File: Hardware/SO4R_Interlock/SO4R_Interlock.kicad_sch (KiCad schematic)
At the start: 143 parts, among them J1 USB-C 2.0 16P, J2 USB-C 2.0 16P, J3 USB-C 2.0 16P, J4 USB-C 2.0 16P, J5 Header 1x3, J6 RJ45_LED_Shielded, J7 8P8C_LED_Shielded_x4, Q1 2N7002, Q2 2N7002, Q3 2N7002, Q4 2N7002, Q5 2N7002, Q6 2N7002, Q7 2N7002, Q8 2N7002, U1 FT230XS, U10 TPD4E02B04DQA, U11 TPD4E02B04DQA, U12 TPD4E02B04DQA, U2 FT230XS, U3 FT230XS, U4 FT230XS, U5 74LVC1G07, U6 74LVC1G07, U7 74LVC1G07, U8 AVR32DB48x-xPT, U9 TPD4E02B04DQA

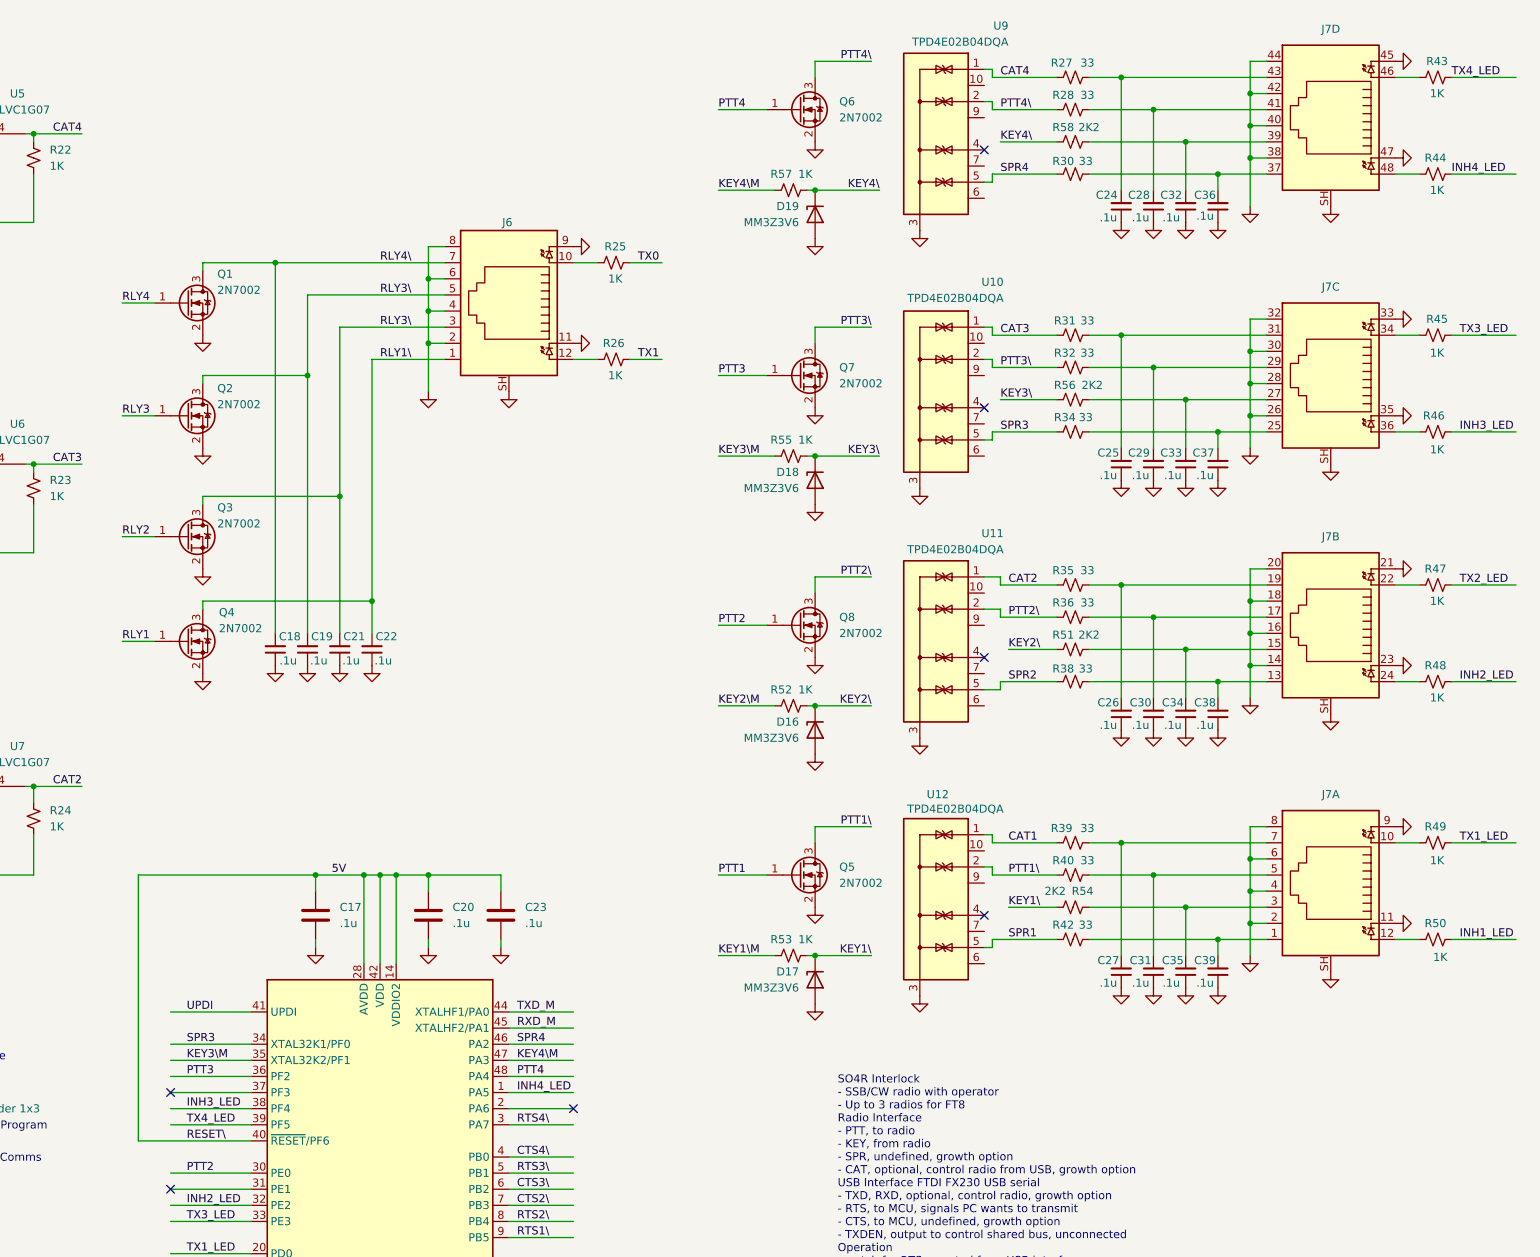
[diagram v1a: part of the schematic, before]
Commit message: reversed the RJ45 connectors
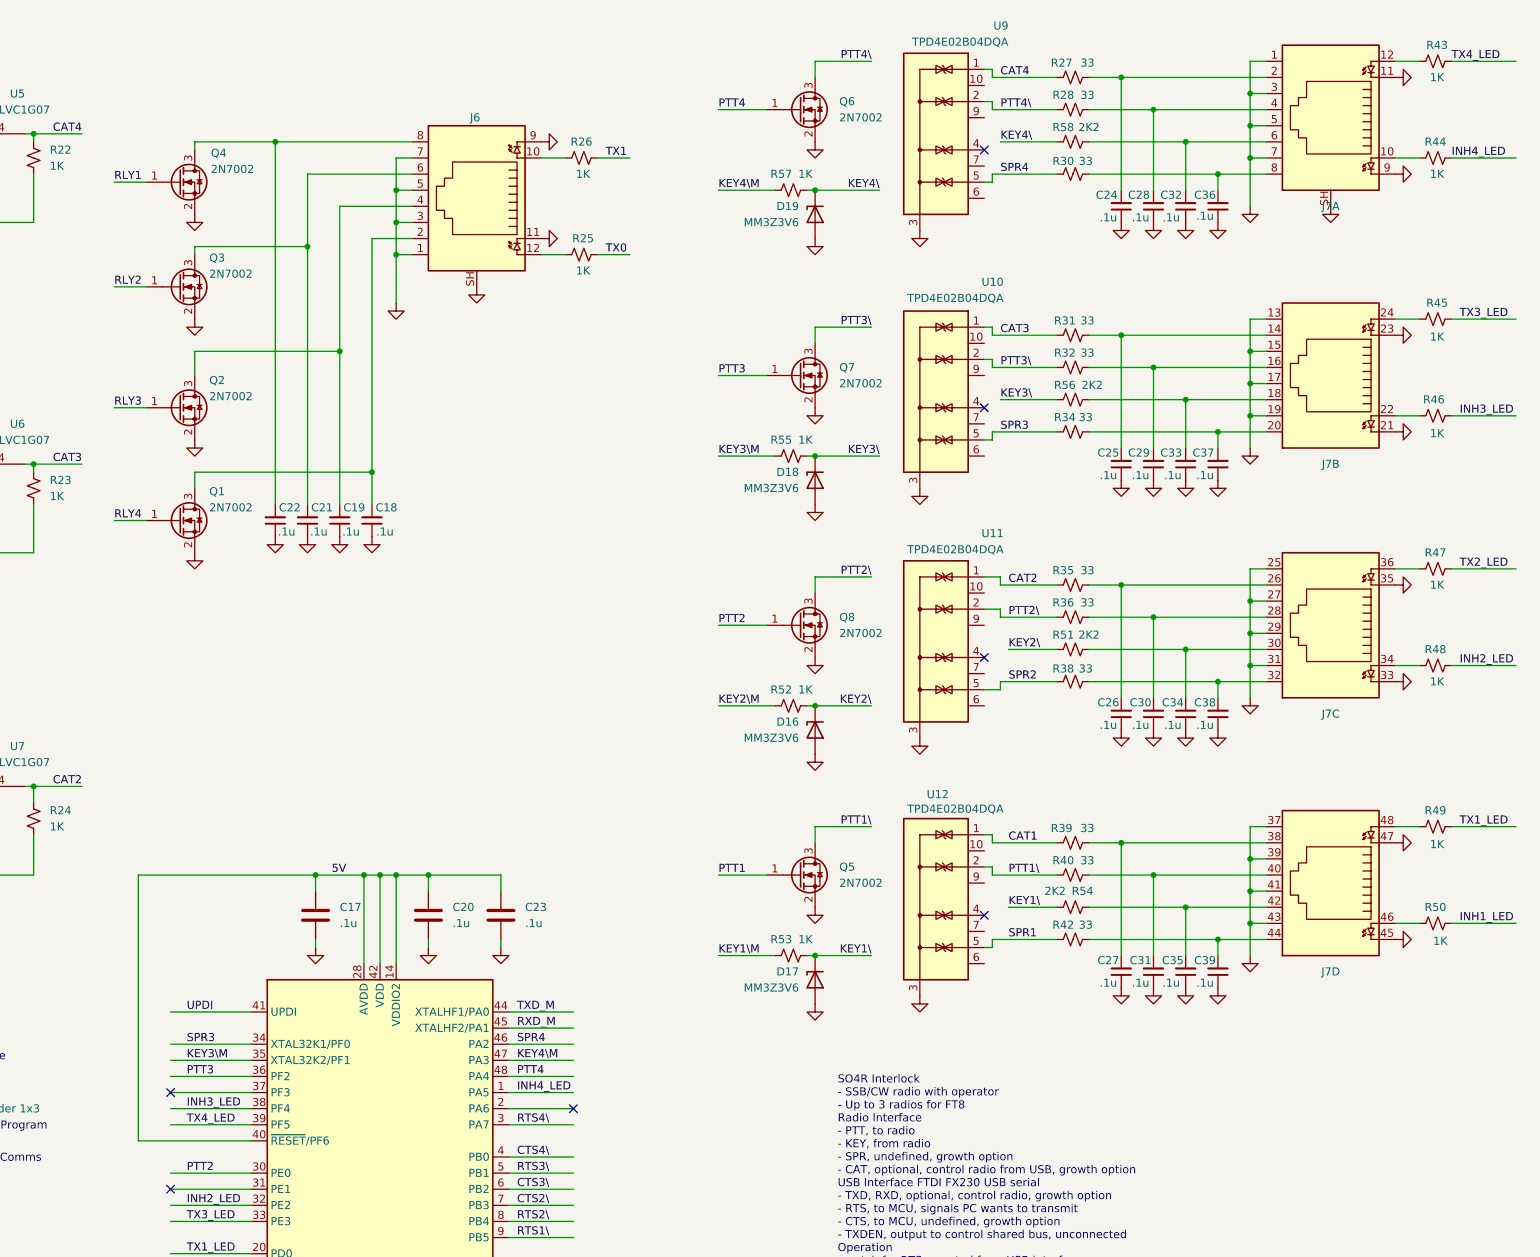
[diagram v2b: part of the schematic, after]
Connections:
- net GND: now also J6.1, J6.3, J6.5, J6.7, J7.1, J7.13, J7.15, J7.17, J7.19, J7.25, J7.27, J7.29, J7.3, J7.31, J7.37, J7.39, J7.41, J7.43, J7.5, J7.7; no longer J6.2, J6.4, J6.6, J6.8, J7.14, J7.16, J7.18, J7.2, J7.20, J7.26, J7.28, J7.30, J7.32, J7.38, J7.4, J7.40, J7.42, J7.44, J7.6, J7.8, J7.SH, J7.SH, J7.SH
- net at C25.2, R31.2: now also J7.14; no longer J7.31
- net at C38.2, R38.2: now also J7.32; no longer J7.13
- net at C34.2, R51.1: now also J7.30; no longer J7.15
- net at C30.2, R36.2: now also J7.28; no longer J7.17
- net at C26.2, R35.2: now also J7.26; no longer J7.19
- net at J7.22: now also R46.1; no longer R47.1
- net at J7.24: now also R45.1; no longer R48.1
- net at C37.2, R34.2: now also J7.20; no longer J7.25
- net at C33.2, R56.1: now also J7.18; no longer J7.27
- net at C29.2, R32.2: now also J7.16; no longer J7.29
- net at J7.34: now also R48.1; no longer R45.1
- net at J7.36: now also R47.1; no longer R46.1
- net at C28.2, R28.2: now also J7.4; no longer J7.41
- net at C27.2, R39.2: now also J7.38; no longer J7.7
- net at C31.2, R40.2: now also J7.40; no longer J7.5
- net at C36.2, R30.2: now also J7.8; no longer J7.37
- net at R43.1: now also J7.12; no longer J7.46
- net at C35.2, R54.1: now also J7.42; no longer J7.3
- net at C39.2, R42.2: now also J7.44; no longer J7.1
- net at R49.1: now also J7.48; no longer J7.10
- net at C24.2, R27.2: now also J7.2; no longer J7.43
- net at R50.1: now also J7.46; no longer J7.12
- net at C32.2, R58.1: now also J7.6; no longer J7.39
- net at R44.1: now also J7.10; no longer J7.48
- net at R26.1: now also J6.10; no longer J6.12
- net at R25.1: now also J6.12; no longer J6.10
- net RLY1\: no longer names the net of C22.2, Q4.3 (D)
- net RLY1\: now also J6.8; no longer J6.1
- removed net RLY3\: C19.2, C21.2, J6.3, J6.5, Q2.3 (D), Q3.3 (D)
- net RLY4\: no longer names the net of C18.2, Q1.3 (D)
- net RLY4\: now also J6.2; no longer J6.7
- new net: C21.2, J6.6, Q3.3 (D)
- new net: C19.2, J6.4, Q2.3 (D)
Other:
- moved on the sheet: C18, C19, C21, C22, J6, J7A, Q1, Q2, Q3, Q4, R25, R26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

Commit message: Manually merged git branch V2 into main
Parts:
- removed C18, C19, C21, C22: .1u, Capacitor_SMD:C_0402_1005Metric, symbol Device:C_Small
- removed Q1, Q2, Q3, Q4: 2N7002, Package_TO_SOT_SMD:SOT-23, symbol Transistor_FET:2N7002
- added C1: .1u, Capacitor_SMD:C_0402_1005Metric, symbol Device:C
- added C18: 100p, Capacitor_SMD:C_0402_1005Metric, symbol Device:C
- added C30, C32, C34, C36, C42, C43, C44, C45: .1u, Capacitor_SMD:C_0402_1005Metric, symbol Device:C_Small
- added D21, D22, D23, D24, D5: BAS316, Diode_SMD:D_SOD-323, symbol Diode:BAS316
- added J1: 12V, Connector_BarrelJack:BarrelJack_Kycon_KLDX-0202-xC_Horizontal, symbol Connector:Conn_Coaxial_Power
- added R25: 4K7, Resistor_SMD:R_0402_1005Metric, symbol Device:R_Small_US
- added R26, R27, R28, R29, R30, R31, R32: 10K, Resistor_SMD:R_0402_1005Metric, symbol Device:R_Small_US
- added R33: 1K2, Resistor_SMD:R_0402_1005Metric, symbol Device:R_Small_US
- added R34: 47k, Resistor_SMD:R_0402_1005Metric, symbol Device:R_Small_US
- added R35, R36, R37: 47K, Resistor_SMD:R_0402_1005Metric, symbol Device:R_Small_US
- added U8: BTS5200-4EKA, Interlock:Infineon_PG-DSO-14-48-EP, symbol Interlock:BTS5200-4EKA
- D1, D2, D3, D4: footprint Diode_SMD:D_SOD-523 -> Diode_SMD:D_SOD-323
- D10: renamed from D9; footprint Diode_SMD:D_SOD-523 -> Diode_SMD:D_SOD-323
- D11: renamed from D10; footprint Diode_SMD:D_SOD-523 -> Diode_SMD:D_SOD-323
- D12: renamed from D11; footprint Diode_SMD:D_SOD-523 -> Diode_SMD:D_SOD-323
- D13: renamed from D12; footprint Diode_SMD:D_SOD-523 -> Diode_SMD:D_SOD-323
- D17: renamed from D19; value MM3Z3V6 -> MM3Z4V7; footprint Diode_SMD:D_SOD-523 -> Diode_SMD:D_SOD-323
- D18: value MM3Z3V6 -> MM3Z4V7; footprint Diode_SMD:D_SOD-523 -> Diode_SMD:D_SOD-323
- D19: renamed from D16; value MM3Z3V6 -> MM3Z4V7; footprint Diode_SMD:D_SOD-523 -> Diode_SMD:D_SOD-323
- D20: renamed from D17; value MM3Z3V6 -> MM3Z4V7; footprint Diode_SMD:D_SOD-523 -> Diode_SMD:D_SOD-323
- renumbered C9 to C10, C10 to C11, C11 to C12, C12 to C13, C13 to C14, C14 to C15, C15 to C16, C16 to C17, C17 to C19, C1 to C2, C23 to C21, C24 to C22, C25 to C23, C26 to C24, C27 to C25, C28 to C26, C29 to C27, C30 to C28, C31 to C29, C2 to C3, C32 to C31, C34 to C35, C35 to C37, C36 to C38, C37 to C39, C3 to C4, C38 to C40, C39 to C41, C4 to C5, C5 to C6, C6 to C7, C7 to C8, C8 to C9, D13 to D14, D14 to D15, D15 to D16, D5 to D6, D6 to D7, D7 to D8, D8 to D9, J1 to J2, J2 to J3, J3 to J4, J4 to J5, J5 to J6, J6 to J7, J7 to J8, Q6 to Q1, Q7 to Q2, Q8 to Q3, Q5 to Q4, R26 to R38, R25 to R39, R57 to R40, R55 to R41, R52 to R42, R53 to R43, R27 to R44, R28 to R45, R58 to R46, R30 to R47, R31 to R48, R32 to R49, R56 to R50, R34 to R51, R35 to R52, R36 to R53, R51 to R54, R38 to R55, R39 to R56, R40 to R57, R54 to R58, R42 to R59, R43 to R60, R44 to R61, R45 to R62, R46 to R63, R47 to R64, R48 to R65, R49 to R66, R50 to R67, U9 to U10, U10 to U11, U11 to U12, U12 to U13, U8 to U9
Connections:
- net CTS2\: now also U9.6 (PB2); no longer U9.7 (PB3)
- net CTS3\: now also U9.5 (PB1); no longer U9.6 (PB2)
- net CTS4\: now also U9.3 (PA7); no longer U9.4 (PB0)
- net GND: now also C1.2, C18.2, C30.1, C32.1, C34.1, C36.1, C42.1, C43.1, C44.1, C45.1, J1.2 (Ext), R33.2, R34.2, R35.2, R36.2, R37.2, U8.11 (GND); no longer J8.1, J8.13, J8.25, J8.37
- net KEY1\: now also U13.4 (IO3)
- net KEY2\: now also U12.4 (IO3)
- net KEY3\: now also U11.4 (IO3)
- net KEY4\: now also U10.4 (IO3)
- net RLY1: now also R30.1
- net RLY2: now also R29.1
- net RLY3: now also R27.1
- net RLY4: now also R28.1
- net RTS1\: now also U9.8 (PB4); no longer U9.9 (PB5)
- net RTS2\: now also U9.7 (PB3); no longer U9.8 (PB4)
- net RTS3\: now also U9.4 (PB0); no longer U9.5 (PB1)
- net RTS4\: now also U9.2 (PA6); no longer U9.3 (PA7)
- net at J7.6: now also C43.2, R35.1, U8.14 (OUT2)
- net at J7.4: now also C45.2, R37.1, U8.1 (OUT0)
- net at J7.8: now also C42.2, R34.1, U8.13 (OUT3)
- net DSEL1: now reaches U9.11 (PC1)
- net DSEL1: now also R32.1
- net IS: now reaches U9.31 (PE1)
- net IS: now also C18.1, R25.1
- net at J7.2: now also C44.2, R36.1, U8.2 (OUT1)
- net CTS1\: no longer names the net of U4.6 (~{CTS})
- net CTS1\: no longer U9.10 (PC0)
- net INH1_LED renamed RIG1GRN
- net INH2_LED renamed RIG2GRN
- net INH3_LED renamed RIG3GRN
- net INH4_LED renamed RIG4GRN
- net TX0 renamed RLYYEL
- net TX1 renamed RLYGRN
- net TX1DEN renamed RLYGRNDEN
- net TX1D_U renamed RLYGRND_U
- net TX1LED/ renamed RLYGRNLED/
- net TX1_LED renamed RIG1YEL
- net TX2_LED renamed RIG2YEL
- net TX3_LED renamed RIG3YEL
- net TX4_LED renamed RIG4YEL
- new net: C32.2, D23.2 (A), J8.13
- new net: C1.1, D5.2 (A), J1.1 (In)
- new net: C34.2, D24.2 (A), J8.25
- new net: R26.2, U8.10 (DEN)
- new net: R31.2, U8.5 (DSEL0)
- new net: R32.2, U8.4 (DSEL1)
- new net: R27.2, U8.7 (IN0)
- new net: R25.2, R33.1, U8.12 (IS)
- new net: C36.2, D22.2 (A), J8.37
- new net: R29.2, U8.8 (IN2)
- new net: C30.2, D21.2 (A), J8.1
- new net: R28.2, U8.6 (IN1)
- new net: R30.2, U8.9 (IN3)
- new net 12V: D21.1 (K), D22.1 (K), D23.1 (K), D24.1 (K), D5.1 (K), U8.15 (VS)
- new net DEN: R26.1, U9.9 (PB5)
- new net DSEL0: R31.1, U9.10 (PC0)
- no-connect marks 33 -> 27
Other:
- moved on the sheet: C22, C23, C24, C25, C26, C27, C28, C29, C31, C33, C35, C37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
